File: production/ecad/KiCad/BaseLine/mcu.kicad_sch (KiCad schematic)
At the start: 24 parts, among them J6 1332645, Q2 AO3400A, Q3 AO3400A, SW1 SW_Push, SW2 SW_Push, U4 ESP32-WROOM-32UE_M113EH6400UH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, U5 CP2102N-A02-GQFN28

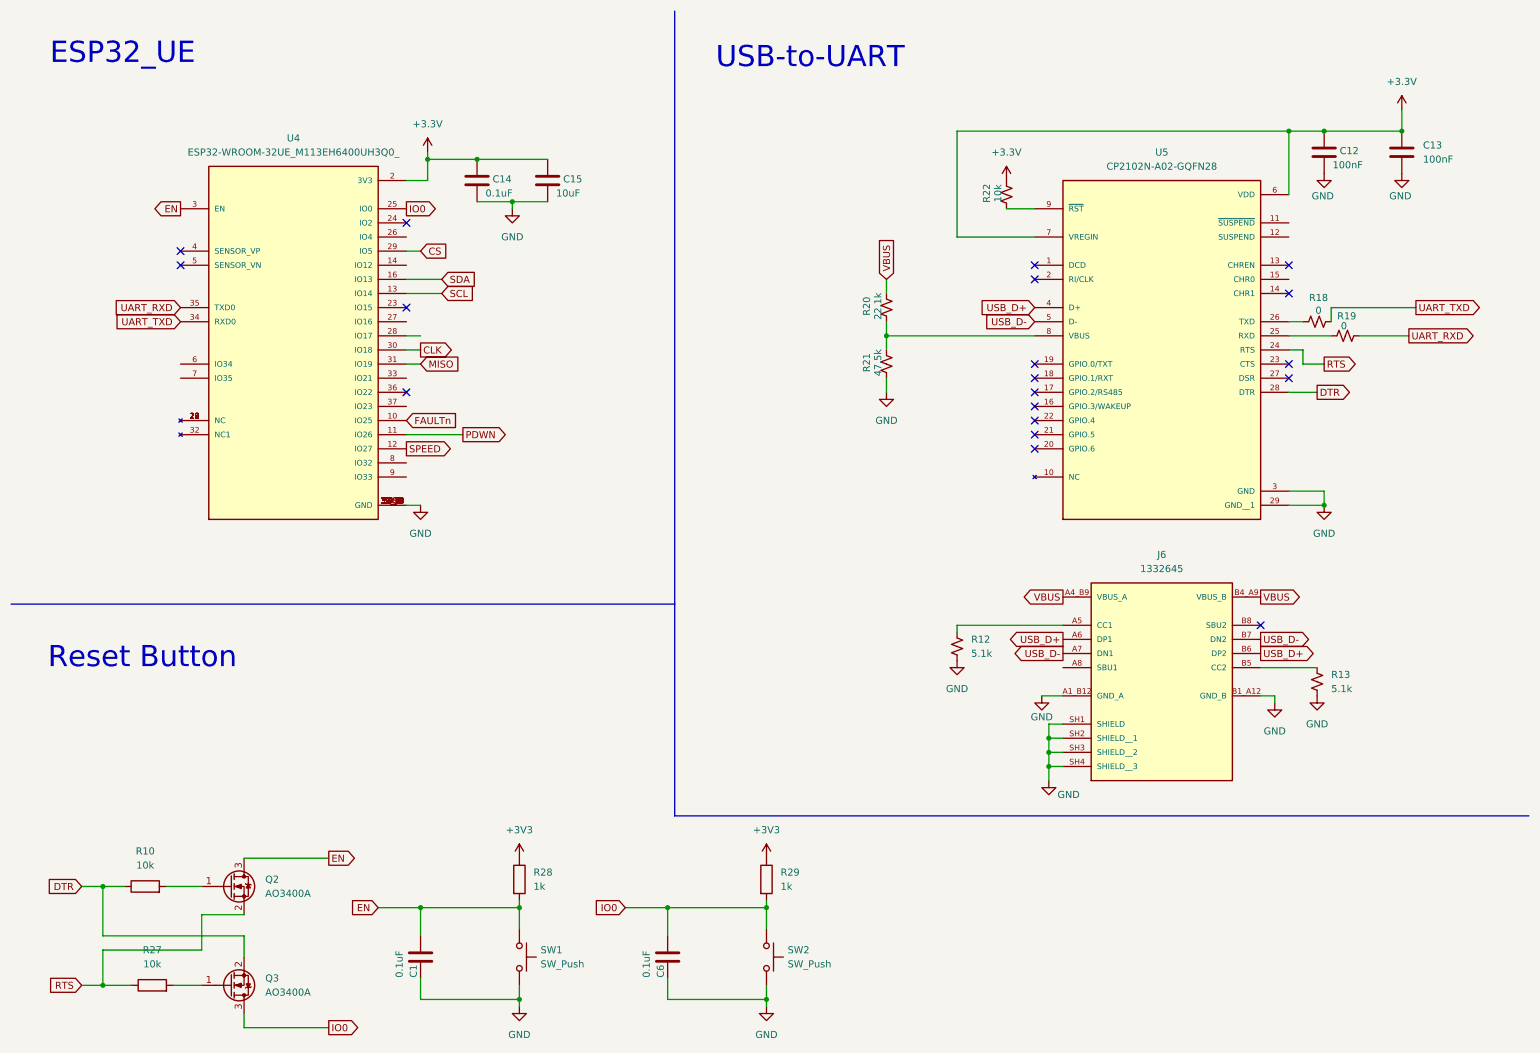
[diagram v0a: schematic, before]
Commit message: Added test points
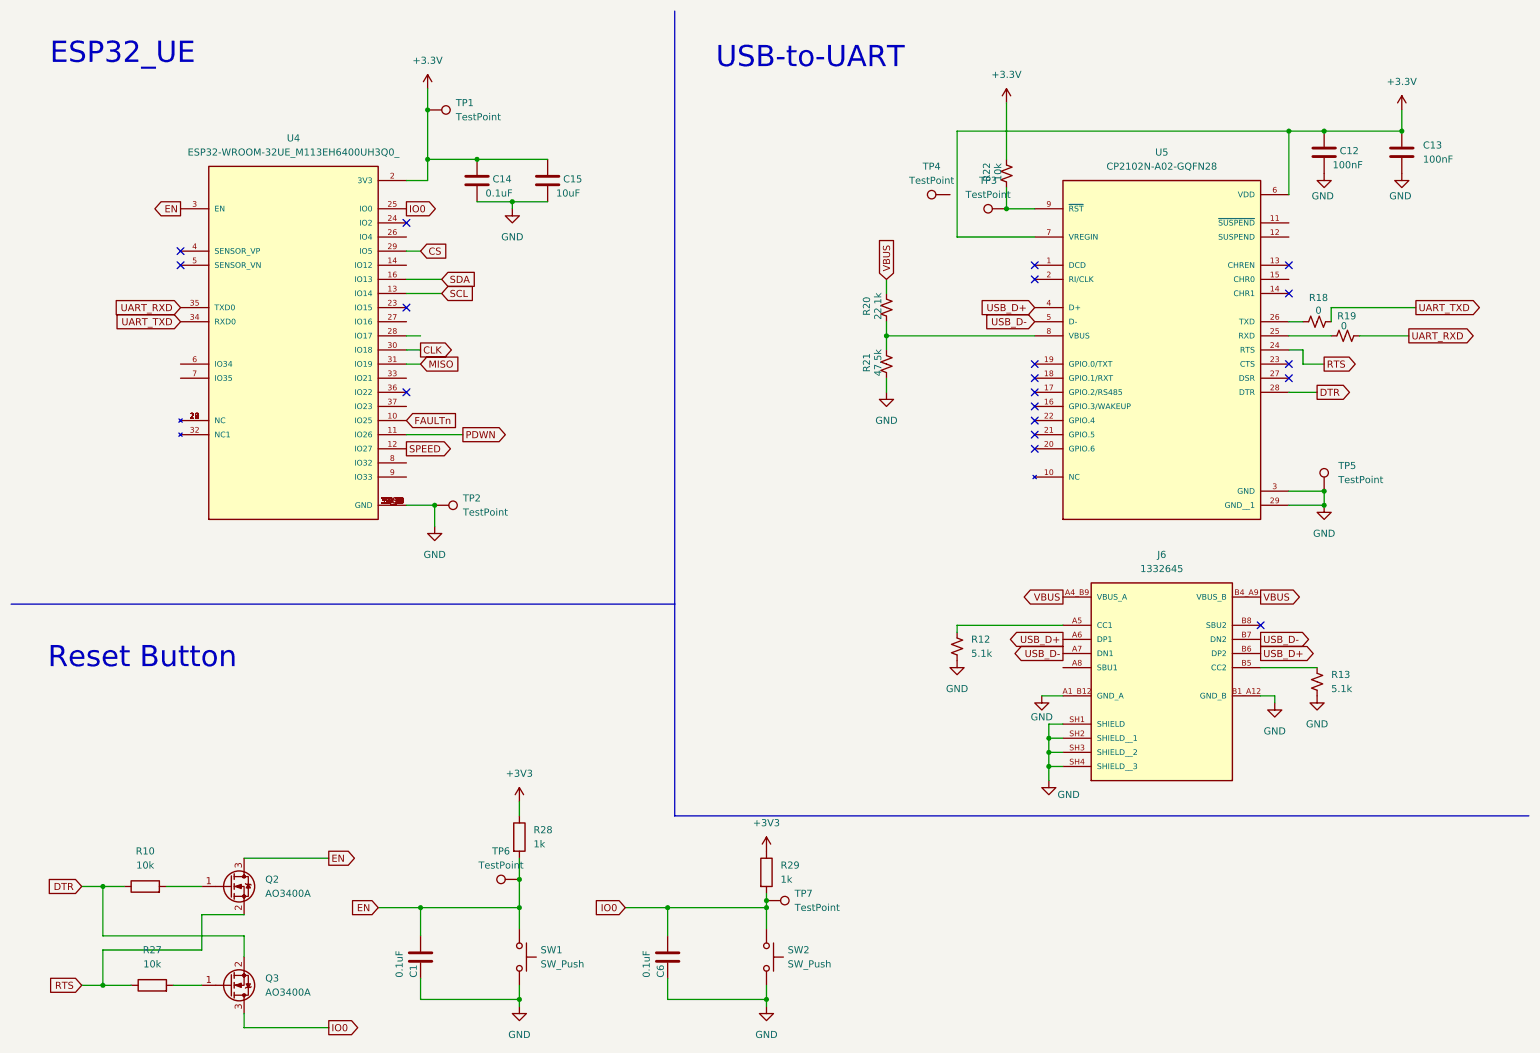
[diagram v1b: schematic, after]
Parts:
- added TP1, TP2, TP3, TP4, TP5, TP6, TP7: TestPoint, symbol Connector:TestPoint
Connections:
- net +3.3V: now also TP1.1
- net EN: now also TP6.1
- net GND: now also TP2.1, TP5.1
- net IO0: now also TP7.1
- net at R22.2, U5.9 (~{RST}): now also TP3.1
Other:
- moved on the sheet: R22, R28, R29

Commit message: Added 0 ohm resistors
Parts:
- added R1, R2, R30, R31, R32, R33, R34, R35, R36, R37: 0, symbol Device:R
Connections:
- net at U4.14 (IO12): now also R2.1
- net at U4.26 (IO4): now also R1.1
- net at U4.27 (IO16): now also R30.1
- net at U4.28 (IO17): now also R31.1
- net at U4.33 (IO21): now also R32.1
- net at U4.37 (IO23): now also R33.1
- net at U4.6 (IO34): now also R36.2
- net at U4.7 (IO35): now also R37.2
- net at U4.8 (IO32): now also R34.1
- net at U4.9 (IO33): now also R35.1
- no-connect marks 19 -> 29

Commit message: Changed annotations
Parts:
- renumbered C1 to C2, C14 to C3, C15 to C4, C6 to C5, C12 to C6, C13 to C7, J6 to J2, Q2 to Q1, Q3 to Q2, R1 to R10, R28 to R11, R2 to R12, R30 to R13, R31 to R14, R32 to R15, R33 to R16, R34 to R17, R35 to R18, R29 to R19, R12 to R22, R22 to R23, R18 to R24, R13 to R25, R19 to R26, R36 to R6, R37 to R7, R10 to R8, R27 to R9, TP6 to TP3, TP7 to TP4, TP4 to TP5, TP3 to TP6, TP5 to TP7, U4 to U2, U5 to U3

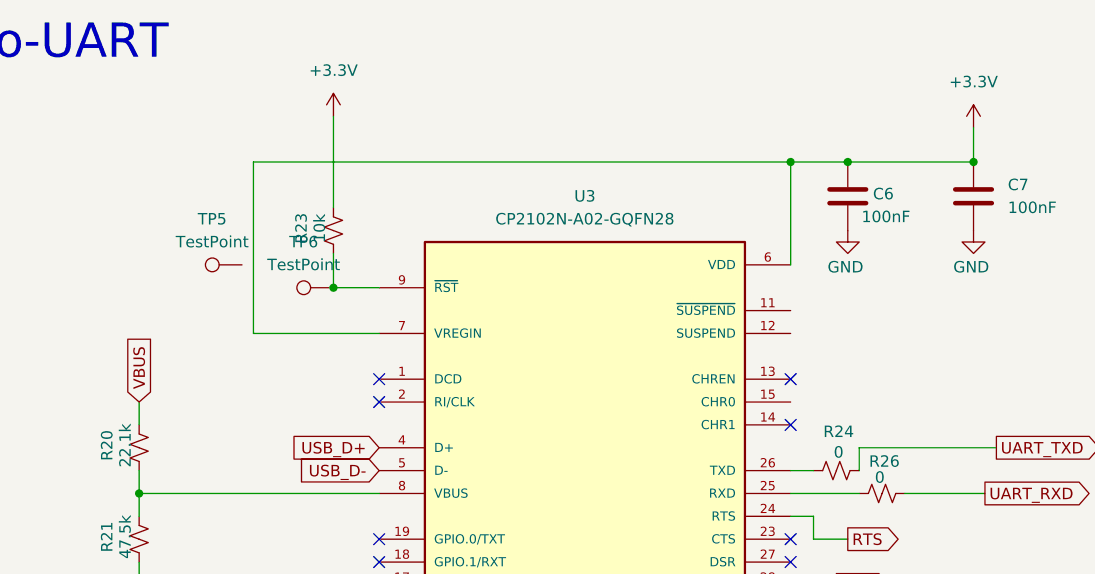
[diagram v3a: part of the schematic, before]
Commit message: Added a couple more 0 ohm resistors
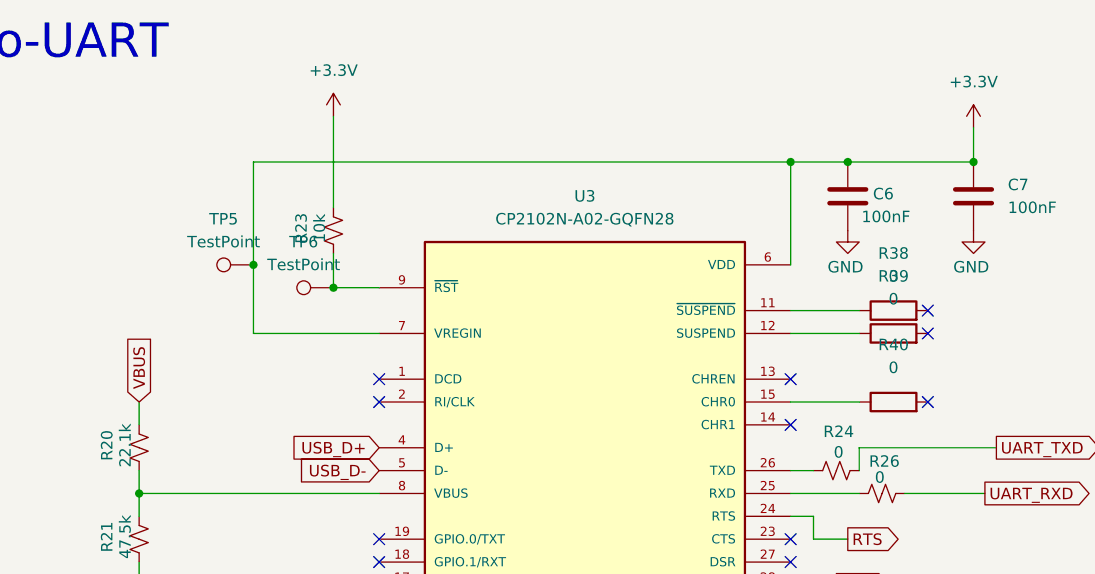
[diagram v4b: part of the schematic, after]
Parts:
- added R38, R39, R40: 0, symbol Device:R
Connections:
- net +3.3V: now also TP5.1
- net at U3.11 (~{SUSPEND}): now also R38.1
- net at U3.12 (SUSPEND): now also R39.1
- net at U3.15 (CHR0): now also R40.1
- no-connect marks 29 -> 32
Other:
- moved on the sheet: TP5

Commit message: More updated annotations and stuff
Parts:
- added R41: 0, symbol Device:R
- renumbered R38 to R27, R39 to R28, R40 to R29
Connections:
- net at J2.A8 (SBU1): now also R41.1
- no-connect marks 32 -> 33
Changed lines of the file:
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@@
 	)
 	(no_connect
+		(at 186.69 132.08)
+	)
+	(no_connect
 		(at 22.86 78.74)
 	)
@@
 	(wire
 		(pts
+			(xy 195.58 118.11) (xy 200.66 118.11)
+		)
+		(stroke
+			(width 0)
+			(type default)
+		)
+	)
+	(wire
+		(pts
 			(xy 92.71 88.9) (xy 82.55 88.9)
 		)
@@
 	(wire
 		(pts
+			(xy 195.58 130.81) (xy 200.66 130.81)
+		)
+		(stroke
+			(width 0)
+			(type default)
+		)
+	)
+	(wire
+		(pts
 			(xy 85.09 186.69) (xy 85.09 190.5)
 		)
@@
 	(wire
 		(pts
+			(xy 194.31 132.08) (xy 195.58 132.08)
+		)
+		(stroke
+			(width 0)
+			(type default)
+		)
+	)
+	(wire
+		(pts
 			(xy 238.76 135.89) (xy 238.76 137.16)
 		)
@@
 	(wire
 		(pts
+			(xy 195.58 132.08) (xy 195.58 130.81)
+		)
+		(stroke
+			(width 0)
+			(type default)
+		)
+	)
+	(wire
+		(pts
 			(xy 82.55 63.5) (xy 88.9 63.5)
 		)
@@
 	(global_label "VBUS"
 		(shape output)
-		(at 200.66 118.11 180)
+		(at 195.58 118.11 180)
 		(fields_autoplaced yes)
 		(effects
@@
 		)
 		(property "Intersheetrefs" "${INTERSHEET_REFS}"
-			(at 192.7762 118.11 0)
+			(at 187.6962 118.11 0)
 			(effects
 				(font
@@
 		(dnp no)
 		(fields_autoplaced yes)
-		(property "Reference" "R38"
+		(property "Reference" "R27"
 			(at 252.73 44.45 90)
 			(effects
@@
 			(project "BaseLine"
 				(path "/ba9eda21-3882-41e1-8265-3d8ac781da20/b5018713-9dac-4933-acc6-88fa6ef21dcb"
-					(reference "R38")
+					(reference "R27")
 					(unit 1)
 				)
@@
 		(dnp no)
 		(fields_autoplaced yes)
-		(property "Reference" "R39"
+		(property "Reference" "R28"
 			(at 252.73 46.99 90)
 			(effects
@@
 			(project "BaseLine"
 				(path "/ba9eda21-3882-41e1-8265-3d8ac781da20/b5018713-9dac-4933-acc6-88fa6ef21dcb"
-					(reference "R39")
+					(reference "R28")
 					(unit 1)
 				)
@@
 	)
 	(symbol
+		(lib_id "Device:R")
+		(at 190.5 132.08 270)
+		(unit 1)
+		(exclude_from_sim no)
+		(in_bom yes)
+		(on_board yes)
+		(dnp no)
+		(fields_autoplaced yes)
+		(property "Reference" "R41"
+			(at 190.5 138.43 90)
+			(effects
+				(font
+					(size 1.27 1.27)
+				)
+			)
+		)
+		(property "Value" "0"
+			(at 190.5 135.89 90)
+			(effects
+				(font
+					(size 1.27 1.27)
+				)
+			)
+		)
+		(property "Footprint" ""
+			(at 190.5 130.302 90)
+			(effects
+				(font
+					(size 1.27 1.27)
+				)
+				(hide yes)
+			)
+		)
+		(property "Datasheet" "~"
+			(at 190.5 132.08 0)
+			(effects
+				(font
+					(size 1.27 1.27)
+				)
+				(hide yes)
+			)
+		)
+		(property "Description" "Resistor"
+			(at 190.5 132.08 0)
+			(effects
+				(font
+					(size 1.27 1.27)
+				)
+				(hide yes)
+			)
+		)
+		(pin "1"
+		)
+		(pin "2"
+		)
+		(instances
+			(project "BaseLine"
+				(path "/ba9eda21-3882-41e1-8265-3d8ac781da20/b5018713-9dac-4933-acc6-88fa6ef21dcb"
+					(reference "R41")
+					(unit 1)
+				)
+			)
+		)
+	)
+	(symbol
 		(lib_id "power:GND")
 		(at 87.63 105.41 0)
@@
 		(dnp no)
 		(fields_autoplaced yes)
-		(property "Reference" "R40"
+		(property "Reference" "R29"
 			(at 252.73 54.61 90)
 			(effects
@@
 			(project "BaseLine"
 				(path "/ba9eda21-3882-41e1-8265-3d8ac781da20/b5018713-9dac-4933-acc6-88fa6ef21dcb"
-					(reference "R40")
+					(reference "R29")
 					(unit 1)
 				)

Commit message: 3.3V supremacy
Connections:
- net +3V3 is gone; now on net +3.3V: R11.1, R19.1
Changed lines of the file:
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@@
 	(wire
 		(pts
+			(xy 147.32 162.56) (xy 147.32 163.83)
+		)
+		(stroke
+			(width 0)
+			(type default)
+		)
+	)
+	(wire
+		(pts
 			(xy 27.94 181.61) (xy 45.72 181.61)
 		)
@@
 	)
 	(symbol
-		(lib_id "power:+3V3")
-		(at 102.87 154.94 0)
-		(unit 1)
-		(exclude_from_sim no)
-		(in_bom yes)
-		(on_board yes)
-		(dnp no)
-		(fields_autoplaced yes)
-		(property "Reference" "#PWR012"
-			(at 102.87 158.75 0)
-			(effects
-				(font
-					(size 1.27 1.27)
-				)
-				(hide yes)
-			)
-		)
-		(property "Value" "+3V3"
-			(at 102.87 149.86 0)
-			(effects
-				(font
-					(size 1.27 1.27)
-				)
-			)
-		)
-		(property "Footprint" ""
-			(at 102.87 154.94 0)
-			(effects
-				(font
-					(size 1.27 1.27)
-				)
-				(hide yes)
-			)
-		)
-		(property "Datasheet" ""
-			(at 102.87 154.94 0)
-			(effects
-				(font
-					(size 1.27 1.27)
-				)
-				(hide yes)
-			)
-		)
-		(property "Description" ""
-			(at 102.87 154.94 0)
-			(effects
-				(font
-					(size 1.27 1.27)
-				)
-				(hide yes)
-			)
-		)
-		(pin "1"
-		)
-		(instances
-			(project "BaseLine"
-				(path "/ba9eda21-3882-41e1-8265-3d8ac781da20/b5018713-9dac-4933-acc6-88fa6ef21dcb"
-					(reference "#PWR012")
-					(unit 1)
-				)
-			)
-		)
-	)
-	(symbol
 		(lib_id "Device:R_Small_US")
 		(at 181.61 127 0)
@@
 	)
 	(symbol
+		(lib_id "power:+3.3V")
+		(at 147.32 162.56 0)
+		(unit 1)
+		(exclude_from_sim no)
+		(in_bom yes)
+		(on_board yes)
+		(dnp no)
+		(fields_autoplaced yes)
+		(property "Reference" "#PWR014"
+			(at 147.32 166.37 0)
+			(effects
+				(font
+					(size 1.27 1.27)
+				)
+				(hide yes)
+			)
+		)
+		(property "Value" "+3.3V"
+			(at 147.32 157.48 0)
+			(effects
+				(font
+					(size 1.27 1.27)
+				)
+			)
+		)
+		(property "Footprint" ""
+			(at 147.32 162.56 0)
+			(effects
+				(font
+					(size 1.27 1.27)
+				)
+				(hide yes)
+			)
+		)
+		(property "Datasheet" ""
+			(at 147.32 162.56 0)
+			(effects
+				(font
+					(size 1.27 1.27)
+				)
+				(hide yes)
+			)
+		)
+		(property "Description" "Power symbol creates a global label with name \"+3.3V\""
+			(at 147.32 162.56 0)
+			(effects
+				(font
+					(size 1.27 1.27)
+				)
+				(hide yes)
+			)
+		)
+		(pin "1"
+		)
+		(instances
+			(project "BaseLine"
+				(path "/ba9eda21-3882-41e1-8265-3d8ac781da20/b5018713-9dac-4933-acc6-88fa6ef21dcb"
+					(reference "#PWR014")
+					(unit 1)
+				)
+			)
+		)
+	)
+	(symbol
 		(lib_id "power:GND")
 		(at 102.87 191.77 0)
@@
 	(symbol
 		(lib_id "power:+3.3V")
-		(at 190.5 29.21 0)
+		(at 102.87 154.94 0)
 		(unit 1)
 		(exclude_from_sim no)
@@
 		(dnp no)
 		(fields_autoplaced yes)
-		(property "Reference" "#PWR018"
-			(at 190.5 33.02 0)
+		(property "Reference" "#PWR012"
+			(at 102.87 158.75 0)
 			(effects
 				(font
@@
 		)
 		(property "Value" "+3.3V"
-			(at 190.5 24.13 0)
+			(at 102.87 149.86 0)
 			(effects
 				(font
@@
 		)
 		(property "Footprint" ""
-			(at 190.5 29.21 0)
+			(at 102.87 154.94 0)
 			(effects
 				(font
@@
 		)
 		(property "Datasheet" ""
-			(at 190.5 29.21 0)
+			(at 102.87 154.94 0)
 			(effects
 				(font
@@
 		)
 		(property "Description" "Power symbol creates a global label with name \"+3.3V\""
-			(at 190.5 29.21 0)
+			(at 102.87 154.94 0)
 			(effects
 				(font
@@
 		)
 		(instances
-			(project ""
+			(project "BaseLine"
 				(path "/ba9eda21-3882-41e1-8265-3d8ac781da20/b5018713-9dac-4933-acc6-88fa6ef21dcb"
-					(reference "#PWR018")
+					(reference "#PWR012")
 					(unit 1)
 				)
@@
 	)
 	(symbol
-		(lib_id "Device:R")
-		(at 252.73 60.96 90)
+		(lib_id "power:+3.3V")
+		(at 190.5 29.21 0)
 		(unit 1)
 		(exclude_from_sim no)
@@
 		(dnp no)
 		(fields_autoplaced yes)
-		(property "Reference" "R29"
-			(at 252.73 54.61 90)
+		(property "Reference" "#PWR018"
+			(at 190.5 33.02 0)
 			(effects
 				(font
 					(size 1.27 1.27)
 				)
+				(hide yes)
 			)
 		)
-		(property "Value" "0"
-			(at 252.73 57.15 90)
+		(property "Value" "+3.3V"
+			(at 190.5 24.13 0)
 			(effects
 				(font
@@
 		)
 		(property "Footprint" ""
-			(at 252.73 62.738 90)
+			(at 190.5 29.21 0)
 			(effects
 				(font
@@
 			)
 		)
-		(property "Datasheet" "~"
-			(at 252.73 60.96 0)
+		(property "Datasheet" ""
+			(at 190.5 29.21 0)
 			(effects
 				(font
@@
 			)
 		)
-		(property "Description" "Resistor"
-			(at 252.73 60.96 0)
+		(property "Description" "Power symbol creates a global label with name \"+3.3V\""
+			(at 190.5 29.21 0)
 			(effects
 				(font
@@
 		(pin "1"
 		)
-		(pin "2"
-		)
 		(instances
-			(project "BaseLine"
+			(project ""
 				(path "/ba9eda21-3882-41e1-8265-3d8ac781da20/b5018713-9dac-4933-acc6-88fa6ef21dcb"
-					(reference "R29")
+					(reference "#PWR018")
 					(unit 1)
 				)
@@
 	)
 	(symbol
-		(lib_id "power:+3V3")
-		(at 147.32 163.83 0)
+		(lib_id "Device:R")
+		(at 252.73 60.96 90)
 		(unit 1)
 		(exclude_from_sim no)
@@
 		(dnp no)
 		(fields_autoplaced yes)
-		(property "Reference" "#PWR014"
-			(at 147.32 167.64 0)
+		(property "Reference" "R29"
+			(at 252.73 54.61 90)
 			(effects
 				(font
 					(size 1.27 1.27)
 				)
-				(hide yes)
 			)
 		)
-		(property "Value" "+3V3"
-			(at 147.32 158.75 0)
+		(property "Value" "0"
+			(at 252.73 57.15 90)
 			(effects
 				(font
@@
 		)
 		(property "Footprint" ""
-			(at 147.32 163.83 0)
+			(at 252.73 62.738 90)
 			(effects
 				(font
@@
 			)
 		)
-		(property "Datasheet" ""
-			(at 147.32 163.83 0)
+		(property "Datasheet" "~"
+			(at 252.73 60.96 0)
 			(effects
 				(font
@@
 			)
 		)
-		(property "Description" ""
-			(at 147.32 163.83 0)
+		(property "Description" "Resistor"
+			(at 252.73 60.96 0)
 			(effects
 				(font
@@
 		(pin "1"
 		)
+		(pin "2"
+		)
 		(instances
 			(project "BaseLine"
 				(path "/ba9eda21-3882-41e1-8265-3d8ac781da20/b5018713-9dac-4933-acc6-88fa6ef21dcb"
-					(reference "#PWR014")
+					(reference "R29")
 					(unit 1)
 				)
